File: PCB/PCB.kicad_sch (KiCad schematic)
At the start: 118 parts, among them J1 Conn_01x02_Pin, J3 Conn_02x16_Odd_Even, J4 USB_C_Receptacle_PowerOnly_6P, SW1 SW_Nidec_CAS-120A1, U1 DRV8833PWPR, U10 TPS63020, U11 TPS63020, U12 TS5A3159ADBVR, U13 CH224K, U2 INA219AxDCN, U3 TPS22917DBV, U4 DRV8833PWP, U5 TPS22917DBV, U9 TP4056-42-ESOP8

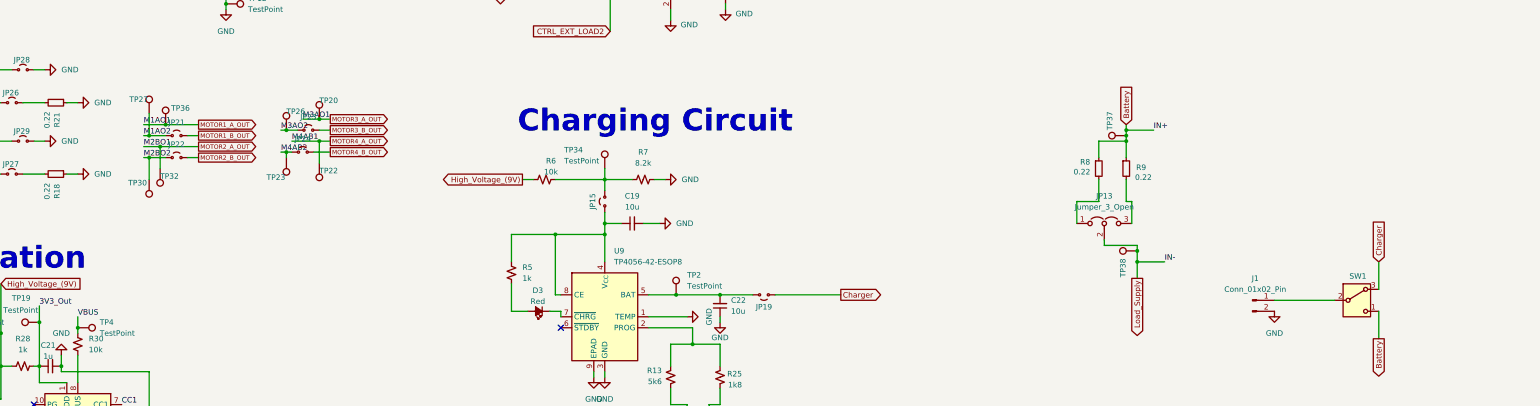
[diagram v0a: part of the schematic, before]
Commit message: Fix PCB layout
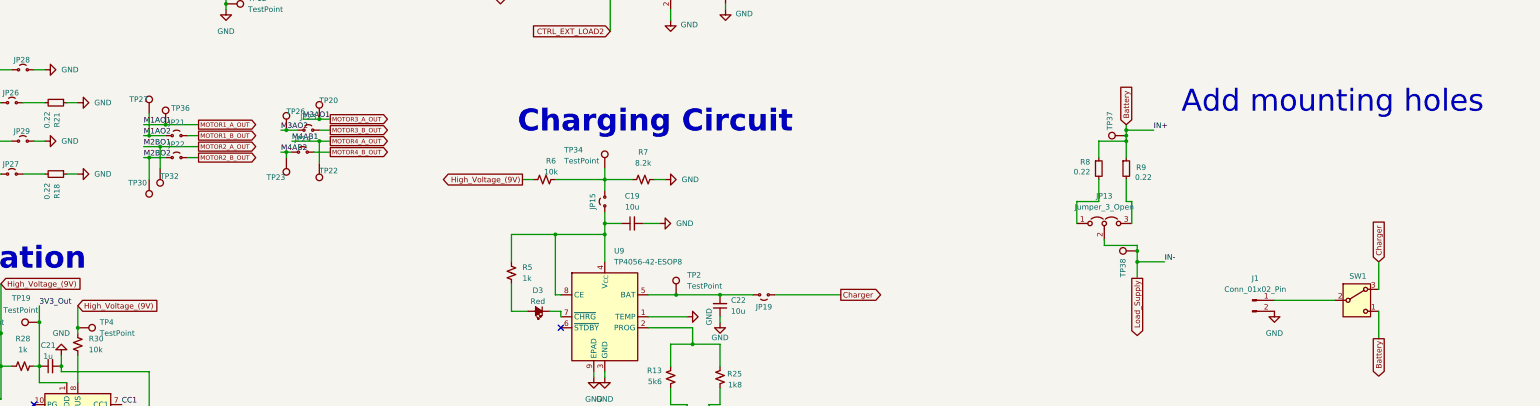
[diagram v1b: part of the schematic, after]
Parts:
- J1: footprint Connector_JST:JST_JWPF_B02B-JWPF-SK-R_1x02_P2.00mm_Vertical -> Connector_JST:JST_PH_S2B-PH-K_1x02_P2.00mm_Horizontal
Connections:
- net VBUS is gone; now on net High_Voltage_(9V): R30.2, TP4.1
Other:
- note added: "Add mounting holes"
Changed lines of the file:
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@@
 		)
 	)
+	(text "Add mounting holes"
+		(exclude_from_sim no)
+		(at 379.222 175.006 0)
+		(effects
+			(font
+				(size 5.08 5.08)
+			)
+		)
+	)
 	(text "Charging Circuit "
 		(exclude_from_sim no)
@@
 	(wire
 		(pts
-			(xy 88.9 224.79) (xy 88.9 227.33)
+			(xy 88.9 222.25) (xy 88.9 227.33)
 		)
 		(stroke
@@
 		)
 	)
-	(label "VBUS"
-		(at 88.9 224.79 0)
-		(effects
-			(font
-				(size 1.27 1.27)
-			)
-			(justify left bottom)
-		)
-	)
 	(label "5V_Out"
 		(at 256.54 27.94 0)
@@
 		)
 	)
+	(global_label "High_Voltage_(9V)"
+		(shape input)
+		(at 88.9 222.25 0)
+		(fields_autoplaced yes)
+		(effects
+			(font
+				(size 1.27 1.27)
+			)
+			(justify left)
+		)
+		(property "Intersheetrefs" "${INTERSHEET_REFS}"
+			(at 109.0603 222.25 0)
+			(effects
+				(font
+					(size 1.27 1.27)
+				)
+				(justify left)
+				(hide yes)
+			)
+		)
+	)
 	(global_label "MOTOR1_CTRL2"
 		(shape output)
@@
 		(polyline
 			(pts
-				(xy 407.67 88.9) (xy 293.37 88.9) (xy 293.37 162.56) (xy 293.37 165.1) (xy 407.67 165.1) (xy 407.67 90.17)
+				(xy 12.065 80.3275) (xy 104.14 80.01) (xy 102.87 12.065) (xy 12.7 12.7)
 			)
 			(stroke
@@
 		(polyline
 			(pts
-				(xy 13.335 198.755) (xy 93.345 198.755) (xy 161.6075 198.755) (xy 162.2425 79.375) (xy 92.075 79.375)
-				(xy 13.335 79.375) (xy 13.335 113.03)
+				(xy 15.24 203.2) (xy 129.54 203.2) (xy 129.54 276.86) (xy 129.54 279.4) (xy 15.24 279.4) (xy 15.24 204.47)
 			)
 			(stroke
@@
 		(polyline
 			(pts
-				(xy 12.065 80.3275) (xy 104.14 80.01) (xy 102.87 12.065) (xy 12.7 12.7)
+				(xy 163.83 168.91) (xy 299.72 167.64) (xy 299.72 240.03) (xy 299.72 278.13) (xy 163.83 278.13) (xy 163.83 170.18)
 			)
 			(stroke
@@
 		(polyline
 			(pts
-				(xy 104.14 12.7) (xy 104.14 78.105) (xy 374.65 78.4224) (xy 374.65 13.0174) (xy 278.13 12.7)
+				(xy 13.335 198.755) (xy 93.345 198.755) (xy 161.6075 198.755) (xy 162.2425 79.375) (xy 92.075 79.375)
+				(xy 13.335 79.375) (xy 13.335 113.03)
 			)
 			(stroke
@@
 		(polyline
 			(pts
-				(xy 15.24 203.2) (xy 129.54 203.2) (xy 129.54 276.86) (xy 129.54 279.4) (xy 15.24 279.4) (xy 15.24 204.47)
+				(xy 407.67 88.9) (xy 293.37 88.9) (xy 293.37 162.56) (xy 293.37 165.1) (xy 407.67 165.1) (xy 407.67 90.17)
 			)
 			(stroke
@@
 		(polyline
 			(pts
-				(xy 163.83 168.91) (xy 299.72 167.64) (xy 299.72 240.03) (xy 299.72 278.13) (xy 163.83 278.13) (xy 163.83 170.18)
+				(xy 104.14 12.7) (xy 104.14 78.105) (xy 374.65 78.4224) (xy 374.65 13.0174) (xy 278.13 12.7)
 			)
 			(stroke
@@
 			)
 		)
-		(property "Footprint" "Connector_JST:JST_JWPF_B02B-JWPF-SK-R_1x02_P2.00mm_Vertical"
+		(property "Footprint" "Connector_JST:JST_PH_S2B-PH-K_1x02_P2.00mm_Horizontal"
 			(at 360.68 220.98 0)
 			(effects

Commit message: Final updates to the INA219, Motor controllers, Voltage regulators and External load switching circuit
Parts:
- removed C11: 10u, Capacitor_SMD:C_0603_1608Metric_Pad1.08x0.95mm_HandSolder, symbol Device:C_Small
- removed C8, C9: 47u, Capacitor_SMD:C_0805_2012Metric_Pad1.18x1.45mm_HandSolder, symbol Device:C_Small
- removed JP18, JP27, JP28: Jumper_2_Small_Open, Jumper:SolderJumper-2_P1.3mm_Open_Pad1.0x1.5mm, symbol Jumper:Jumper_2_Small_Open
- removed R18, R21: 0.22, Resistor_SMD:R_0603_1608Metric_Pad0.98x0.95mm_HandSolder, symbol Device:R_Small
- removed R31: 10k, Resistor_SMD:R_0805_2012Metric_Pad1.20x1.40mm_HandSolder, symbol Device:R_Small
- removed TP10, TP11, TP13, TP14, TP23, TP26, TP27, TP30, TP6, TP7, TP8, TP9: TestPoint, TestPoint:TestPoint_Pad_D1.0mm, symbol Connector:TestPoint
- added C18, C20: 2.2u, Capacitor_SMD:C_0603_1608Metric_Pad1.08x0.95mm_HandSolder, symbol Device:C_Small
- added C23, C24, C25: 10u, Capacitor_SMD:C_0603_1608Metric_Pad1.08x0.95mm_HandSolder, symbol Device:C_Small
- added C27, C28, C29, C30, C31, C32: 22u, Capacitor_SMD:C_0603_1608Metric_Pad1.08x0.95mm_HandSolder, symbol Device:C_Small
- added JP27, JP28: Jumper_3_Open, Jumper:SolderJumper-3_P1.3mm_Open_Pad1.0x1.5mm, symbol Jumper:Jumper_3_Open
- added JP30, JP31, JP32: Jumper_2_Small_Open, Jumper:SolderJumper-2_P1.3mm_Open_Pad1.0x1.5mm, symbol Jumper:Jumper_2_Small_Open
- added R33: 510k, Resistor_SMD:R_0603_1608Metric_Pad0.98x0.95mm_HandSolder, symbol Device:R_Small
- C13, C16, C17: value 2.2u -> 10u; LCSC C23630 -> C19702
- C14: value 10u -> 2.2u; LCSC C19702 -> C23630
- C19, C22: LCSC C19702 -> C19702
- R10: value 200 -> 56k; footprint Resistor_SMD:R_0805_2012Metric_Pad1.20x1.40mm_HandSolder -> Resistor_SMD:R_0603_1608Metric_Pad0.98x0.95mm_HandSolder; LCSC C2933534 -> C23206
- R11: value 100 -> 82k; LCSC C22775 -> C23254
- R2: value 1.8k -> 510k; footprint Resistor_SMD:R_0603_1608Metric -> Resistor_SMD:R_0603_1608Metric_Pad0.98x0.95mm_HandSolder; LCSC C4177 -> C23192
- R32: value 10k -> 510k; footprint Resistor_SMD:R_0805_2012Metric_Pad1.20x1.40mm_HandSolder -> Resistor_SMD:R_0603_1608Metric_Pad0.98x0.95mm_HandSolder; LCSC C17414 -> C23192
- R4: value 560 -> 470k; footprint Resistor_SMD:R_0603_1608Metric -> Resistor_SMD:R_0805_2012Metric_Pad1.20x1.40mm_HandSolder; LCSC C23204 -> C17709
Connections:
- net BISEN2 is gone; now on net SEN2: U4.6 (BISEN)
- net 3V3_Out: no longer J3.18 (Pin_18), JP11.2 (B), TP35.1
- net 5V Out: now also C6.1, C7.1, J3.20 (Pin_20), JP17.1 (A), R2.1, U3.1 (VIN), U3.4 (CT), U5.1 (VIN), U5.4 (CT), JP27.3 (B), JP28.3 (B)
- net Battery: now also C12.1, C16.1, C17.1, U1.1 (~{SLEEP}), U10.10 (VIN2), U10.11 (VIN1), U11.10 (VIN2), U11.11 (VIN1), U4.1 (~{SLEEP}), C23.1, JP27.1 (A), JP28.1 (A)
- net EXT_LOAD1_OUT: now also C25.2; no longer U3.5 (QOD)
- net EXT_LOAD2_OUT: now also C24.2; no longer U5.5 (QOD)
- net GND: now also C13.2, C14.1, C16.2, C17.2, U3.5 (QOD), U5.5 (QOD), C23.2, C24.1, C25.1, C27.2, C28.2, C29.2, C30.2, C31.2, C32.2; no longer C13.1, C14.2, JP29.2 (B)
- net Load_Supply: no longer C12.1, C14.1, C16.1, C3.1, U1.12 (VM), U10.10 (VIN2), U10.11 (VIN1), U11.10 (VIN2), U11.11 (VIN1), U4.12 (VM)
- net at JP26.2 (B): now also R32.2, TP35.1, U11.4 (VOUT1), C27.1, C28.1, C29.1
- net at U1.11 (VCP): now also C18.1; no longer C16.2
- net at R16.2: now also JP32.1 (A); no longer U4.8 (~{FAULT})
- net at U10.14 (PG): now also JP30.1 (A), R33.1; no longer R20.2
- net at JP17.2 (B), TP33.1, U10.4 (VOUT1): now also C30.1, C31.1, C32.1, R33.2
- net at U4.11 (VCP): now also C20.1; no longer C17.2
- net at R32.1, U11.14 (PG): now also JP29.1 (A); no longer R19.2
- net at R14.2: now also JP31.1 (A); no longer U1.8 (~{FAULT})
- removed net 5V_Out: C6.1, C7.1, J3.20 (Pin_20), JP17.1 (A), R2.1, R4.1, U1.1 (~{SLEEP}), U3.1 (VIN), U3.4 (CT), U4.1 (~{SLEEP}), U5.1 (VIN), U5.4 (CT)
- net AISEN1 renamed SEN1
- net SEN1: now also U1.6 (BISEN)
- net AISEN2 renamed SEN2
- net SEN2: now also JP20.1 (A), JP25.1 (A)
- net AISEN3 renamed 3V3 Out
- net 3V3 Out: now also J3.18 (Pin_18), JP11.2 (B), R4.1
- removed net BISEN1: JP20.1 (A), JP25.1 (A), JP29.1 (A), U1.6 (BISEN)
- new net: C18.2, C3.1, JP27.2 (C), U1.12 (VM)
- new net: JP31.2 (B), U1.8 (~{FAULT})
- new net: JP29.2 (B), R19.2
- new net: C13.1, C20.2, JP28.2 (C), U4.12 (VM)
- new net: C14.2, U4.14 (VINT)
- new net: JP32.2 (B), U4.8 (~{FAULT})
- new net: JP30.2 (B), R20.2
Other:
- note added: "Fault Checking"
- note added: "Giving option for motors to be supplied by the 5V or battery supply"
- note added: "Sensor resistor"
- note added: "TEST: Test voltage at feedback"
- note added: "TEST: motor current and voltage"
- note added: "TEST: output current"
- note added: "TEST: shunt voltage"
- note added: "inductor: lower ripple current, smoother operation and best because of low current"
- moved on the sheet: C10, C12, C15, C2, C3, D1, D2, D4, D5, JP10, JP17, JP9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

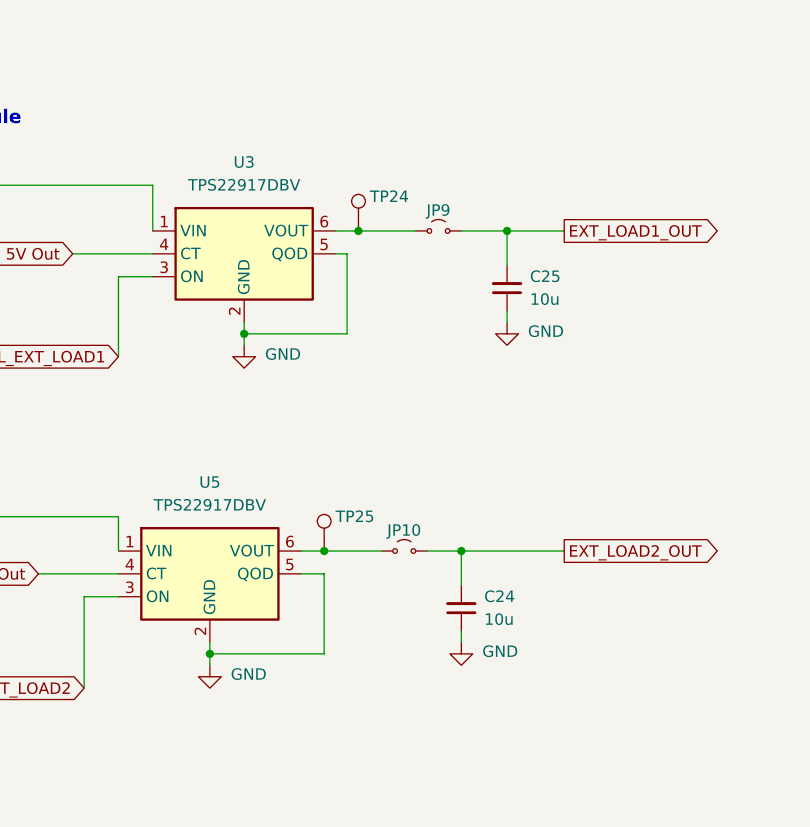
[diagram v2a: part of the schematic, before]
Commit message: Addition of the RQOD resistor
The resistor between the QOD and VOUT pins was mistakenly omitted.
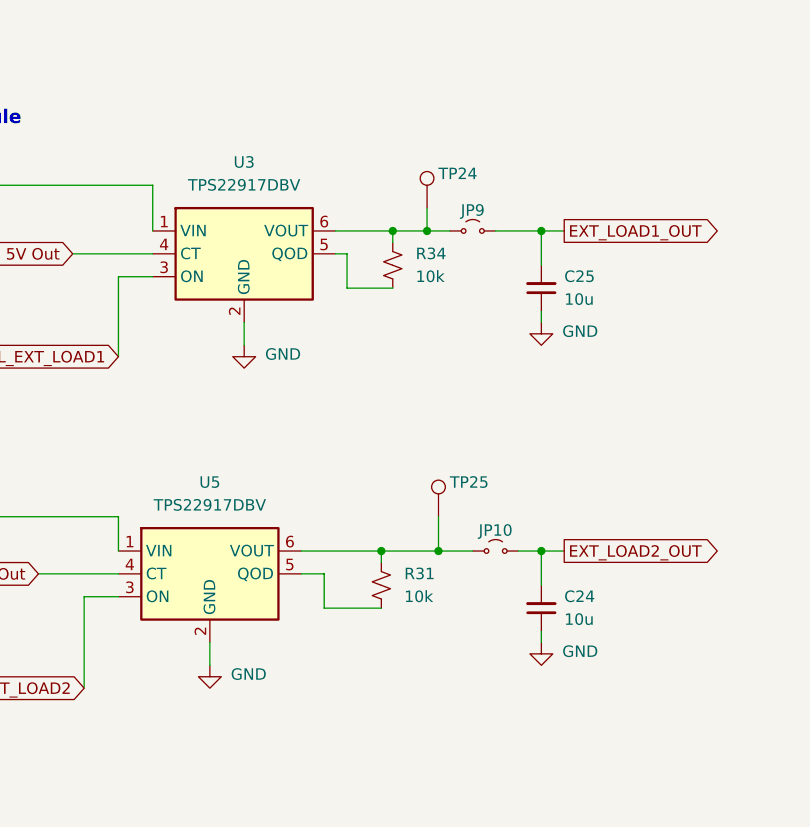
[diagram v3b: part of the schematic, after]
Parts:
- added R31, R34: 10k, Resistor_SMD:R_0805_2012Metric_Pad1.20x1.40mm_HandSolder, symbol Device:R_Small_US
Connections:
- net GND: no longer U3.5 (QOD), U5.5 (QOD)
- net at JP10.1 (A), TP25.1, U5.6 (VOUT): now also R31.2
- net at JP9.1 (A), TP24.1, U3.6 (VOUT): now also R34.2
- new net: R34.1, U3.5 (QOD)
- new net: R31.1, U5.5 (QOD)
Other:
- moved on the sheet: C24, C25, JP10, JP9, TP24, TP25

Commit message: Final Component checks before routing
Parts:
- removed C18, C20: 2.2u, Capacitor_SMD:C_0603_1608Metric_Pad1.08x0.95mm_HandSolder, symbol Device:C_Small
- removed C4: 1u, Capacitor_SMD:C_0603_1608Metric_Pad1.08x0.95mm_HandSolder, symbol Device:C_Small
- added C11, C8, C9: 100n, Capacitor_SMD:C_0603_1608Metric_Pad1.08x0.95mm_HandSolder, symbol Device:C_Small
- C5: value 0.1u -> 100n
- R8, R9: LCSC C2960770 -> C3013347
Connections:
- net M2AO1 is gone; now on net MOTOR2_A_OUT: U1.7 (BOUT1)
- net M2AO2 is gone; now on net M2BO2: U1.5 (BOUT2)
- net Battery: now also C8.1
- net Load_Supply: now also C8.2
- net at C3.1, JP27.2 (C), U1.12 (VM): now also C11.1
- net at U1.11 (VCP): now also C11.2
- net at U4.11 (VCP): now also C9.2
- net at C13.1, JP28.2 (C), U4.12 (VM): now also C9.1
- net M4AB2 renamed M4BO2

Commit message: Placing All components onto the silkscreen
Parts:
- removed JP11, JP12, JP14, JP16, JP20, JP25, JP29, JP30, JP31, JP32: Jumper_2_Small_Open, Jumper:SolderJumper-2_P1.3mm_Open_Pad1.0x1.5mm, symbol Jumper:Jumper_2_Small_Open
- removed JP13, JP27, JP28: Jumper_3_Open, Jumper:SolderJumper-3_P1.3mm_Open_Pad1.0x1.5mm, symbol Jumper:Jumper_3_Open
- removed TP12: TestPoint, TestPoint:TestPoint_Pad_D1.0mm, symbol Connector:TestPoint
- added R12: 0.22, Resistor_SMD:R_0603_1608Metric_Pad0.98x0.95mm_HandSolder, symbol Device:R_Small
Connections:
- net 3V3_VOUT2 is gone; now on an unnamed net: U11.5 (VOUT2)
- net 5V_VOUT2 is gone; now on an unnamed net: U10.5 (VOUT2)
- net 5V Out: now also C11.1, C13.1, C3.1, C9.1, U1.12 (VM), U4.12 (VM)
- net Battery: now also R12.1; no longer C12.1, C16.1, C17.1, C23.1, U10.10 (VIN2), U10.11 (VIN1), U11.10 (VIN2), U11.11 (VIN1)
- net Load_Supply: now also C12.1, C16.1, C17.1, C23.1, R8.2, R9.2, U10.10 (VIN2), U10.11 (VIN1), U11.10 (VIN2), U11.11 (VIN1), R12.2
- net SEN1: now also R23.2
- net SEN2: now also R22.2
- net at R14.2: now also U1.8 (~{FAULT})
- net at R16.2: now also U4.8 (~{FAULT})
- net at R33.1, U10.14 (PG): now also R20.2
- net at R32.1, U11.14 (PG): now also R19.2

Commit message: Routing
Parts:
- removed U12: TS5A3159ADBVR, Mix:SOT-23-6_L2.9-W1.6-P0.95-LS2.8-BR, symbol Analog_Switch:TS5A3159ADBVR
- added JP20, JP25: Jumper_2_Small_Open, Jumper:SolderJumper-2_P1.3mm_Open_Pad1.0x1.5mm, symbol Jumper:Jumper_2_Small_Open
- added U6: TS5A3159ADBVR, Mix:SOT-23-6_L2.9-W1.6-P0.95-LS2.8-BR, symbol Symbols:TS5A3159ADBVR
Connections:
- net 3V3 Out: now also JP20.1 (A)
- net 3V3_Out: now also JP25.2 (B); no longer C21.1, R28.2, U13.1 (VDD)
- net FAST_CHARGE_CTRL: now also U6.6 (IN)
- net GND: now also R13.1, R25.1, U6.2 (GND)
- net at R25.2: now also U6.1 (NO)
- net at R13.2: now also U6.3 (NC)
- new net: C21.1, JP25.1 (A), R28.2, U13.1 (VDD)
- new net: JP20.2 (B), U6.5 (V+)
- new net: U6.4 (COM), U9.2 (PROG)
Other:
- moved on the sheet: C19, C22, D3, JP15, JP19, R13, R25, R5, R6, R7, TP19, TP2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

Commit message: Final Schematic edits
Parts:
- removed C19, C22: 10u, Capacitor_SMD:C_0603_1608Metric_Pad1.08x0.95mm_HandSolder, symbol Device:C_Small
- removed C21: 1u, Capacitor_SMD:C_0603_1608Metric_Pad1.08x0.95mm_HandSolder, symbol Device:C_Small
- removed D3: Red, LED_SMD:LED_0603_1608Metric_Pad1.05x0.95mm_HandSolder, symbol Device:LED_Small_Filled
- removed J1: Conn_01x02_Pin, Connector_JST:JST_PH_S2B-PH-K_1x02_P2.00mm_Horizontal, symbol Connector:Conn_01x02_Pin
- removed J4: USB_C_Receptacle_PowerOnly_6P, Mix:USB-C-SMD_TYPE-602-T3, symbol Connector:USB_C_Receptacle_PowerOnly_6P
- removed JP15, JP19, JP20, JP25: Jumper_2_Small_Open, Jumper:SolderJumper-2_P1.3mm_Open_Pad1.0x1.5mm, symbol Jumper:Jumper_2_Small_Open
- removed R13: 5k6, Resistor_SMD:R_0805_2012Metric_Pad1.20x1.40mm_HandSolder, symbol Device:R_Small_US
- removed R22: 0.22, Resistor_SMD:R_0603_1608Metric_Pad0.98x0.95mm_HandSolder, symbol Device:R_Small
- removed R25: 1k8, Resistor_SMD:R_0603_1608Metric_Pad0.98x0.95mm_HandSolder, symbol Device:R_Small_US
- removed R28, R5: 1k, Resistor_SMD:R_0603_1608Metric_Pad0.98x0.95mm_HandSolder, symbol Device:R_Small_US
- removed R29: 6k8, Resistor_SMD:R_0805_2012Metric_Pad1.20x1.40mm_HandSolder, symbol Device:R_Small_US
- removed R30, R6: 10k, Resistor_SMD:R_0805_2012Metric_Pad1.20x1.40mm_HandSolder, symbol Device:R_Small_US
- removed R7: 8.2k, Resistor_SMD:R_0805_2012Metric_Pad1.20x1.40mm_HandSolder, symbol Device:R_Small_US
- removed SW1: SW_Nidec_CAS-120A1, Mix:SW-TH_1MS1T1B1M1QES-5, symbol Switch:SW_Nidec_CAS-120A1
- removed TP19, TP2, TP3, TP34, TP4: TestPoint, TestPoint:TestPoint_Pad_D1.0mm, symbol Connector:TestPoint
- removed U13: CH224K, Mix:ESSOP-10_L4.9-W3.9-P1.0-LS6.0-TL-EP, symbol Interface_USB:CH224K
- removed U6: TS5A3159ADBVR, Mix:SOT-23-6_L2.9-W1.6-P0.95-LS2.8-BR, symbol Symbols:TS5A3159ADBVR
- removed U9: TP4056-42-ESOP8, Mix:ESOP-8_L4.9-W3.9-P1.27-LS6.0-BL-EP, symbol Battery_Management:TP4056-42-ESOP8
- added R30: 0.22, Resistor_SMD:R_0603_1608Metric_Pad0.98x0.95mm_HandSolder, symbol Device:R_Small
- U10, U11: value TPS63020 -> TPS63020DSJR
- U2: value INA219AxDCN -> INA219AIDCNR
- U4: value DRV8833PWP -> DRV8833PWPR
- renumbered C30 to C31, C31 to C32, C32 to C33, C23 to C34, J3 to J4, JP17 to JP18, R19 to R23, R23 to R25, R27 to R28, R20 to R29, R16 to R41
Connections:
- net GND: now also R30.1
- net SEN1: no longer names the net of R25.2, U1.3 (AISEN), U1.6 (BISEN)
- net SEN2: no longer names the net of U4.3 (AISEN), U4.6 (BISEN)
- net SEN2: now also R30.2
- no-connect marks 10 -> 3
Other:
- removed sheet AMOS's Section
- added sheet AMOS's Section1 (AMOS's section.kicad_sch)
- note added: "Ability to change R1 in feedback of the voltaged regulator"
- note added: "Battery monitoring module Utilises an INA219 IC in the SOT-23 package."
- note added: "Connector"
- note added: "EN pin tied to GND via a capacitor: This will ensure the regulator is disabled until you supply the input voltage, at which point the regulator will turn on automatically. PS/SYNC pin tied to GND via a capacitor: This ensures the regulator operates in Power Save Mode, which is generally useful for light-load efficiency. VINA pin tied to the power source: This is essential because it provides the 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"
- note added: "Fault Checking LED"
- note added: "Jumpers used to measre output current. Test Points are used to measure output voltage."
- note added: "Motor Controller Module"
- note added: "ON pin toggles the switch to be ON or OFF. CT pin controls the slew rate of the switch."
- note added: "Power Flags"
- note added: "Shunt resistor configuration."
- note added: "TP37 & TP38 are used to measure the shunt voltage."
- note removed: "Add mounting holes"
- note removed: "Battery monitoring module Utilises an INA219 IC in the SOT-23 pacjage."
- note removed: "Charging Circuit"
- note removed: "Giving option for motors to be supplied by the 5V or battery supply"
- note removed: "Motor Controller MOdule"
- note removed: "Sensor resistor"
- note removed: "TEST: motor current and voltage"
- note removed: "TEST: output current"
- note removed: "TEST: shunt voltage"
- note removed: "USb Integration"
- moved on the sheet: C10, C11, C12, C13, C14, C15, C16, C17, C2, C24, C25, C27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
